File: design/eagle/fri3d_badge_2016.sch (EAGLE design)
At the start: 45 parts

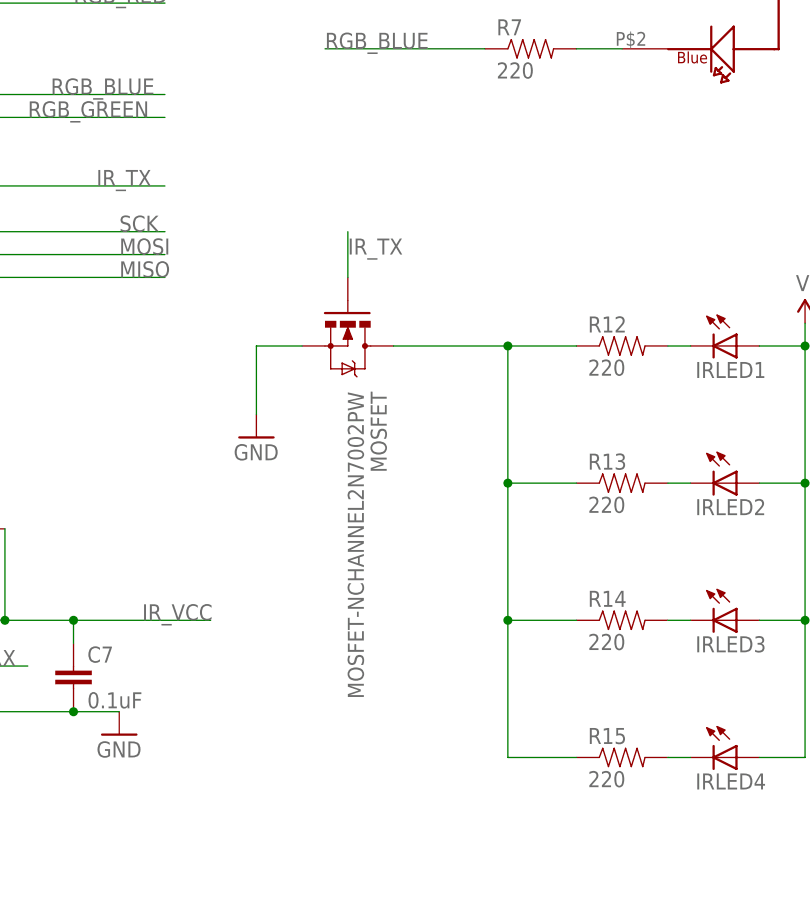
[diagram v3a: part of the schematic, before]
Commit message: fixed MOSFET footprint + added dots for diodes
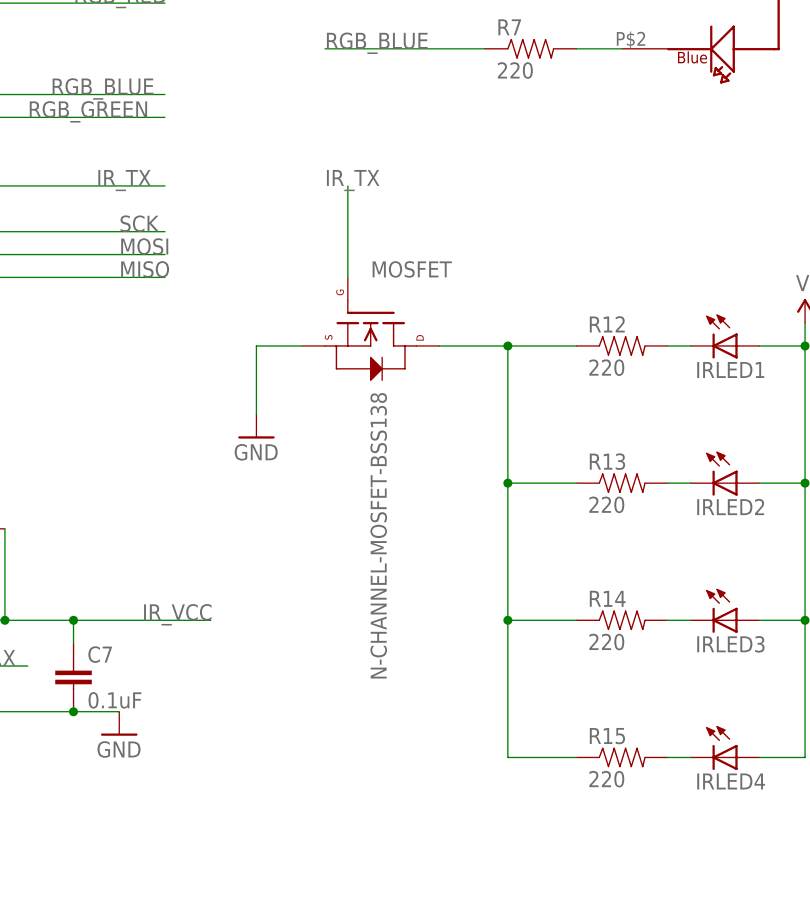
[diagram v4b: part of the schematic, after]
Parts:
- MOSFET: value MOSFET-NCHANNEL2N7002PW -> N-CHANNEL-MOSFET-BSS138; device SparkFun-DiscreteSemi:MOSFET-NCHANNEL2N7002PW -> GeekAmmo:N-CHANNEL-MOSFET-BSS138
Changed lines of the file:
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@@
 <attributes>
 <attribute name="CNAME" value="Fri3d Camp Badge"/>
-<attribute name="CREVISION" value="4"/>
+<attribute name="CREVISION" value="6"/>
 <attribute name="DESIGNER" value="Christophe VG"/>
 </attributes>
@@
 <part name="R14" library="SparkFun-Passives" deviceset="RESISTOR" device="0805-RES" value="220"/>
 <part name="R15" library="SparkFun-Passives" deviceset="RESISTOR" device="0805-RES" value="220"/>
-<part name="MOSFET" library="SparkFun-DiscreteSemi" deviceset="MOSFET-NCHANNEL" device="2N7002PW"/>
 <part name="R5" library="SparkFun-Passives" deviceset="RESISTOR" device="0805-RES" value="220"/>
 <part name="R6" library="SparkFun-Passives" deviceset="RESISTOR" device="0805-RES" value="220"/>
@@
 <part name="SUPPLY9" library="SparkFun-Aesthetics" deviceset="VCC" device=""/>
 <part name="GND13" library="SparkFun-Aesthetics" deviceset="GND" device=""/>
+<part name="MOSFET" library="GeekAmmo" deviceset="N-CHANNEL-MOSFET" device="-BSS138"/>
 </parts>
 <sheets>
@@
 <instance part="R14" gate="G$1" x="193.04" y="40.64"/>
 <instance part="R15" gate="G$1" x="193.04" y="25.4"/>
-<instance part="MOSFET" gate="G$1" x="162.56" y="71.12" rot="R270"/>
 <instance part="R5" gate="G$1" x="205.74" y="154.94"/>
 <instance part="R6" gate="G$1" x="119.38" y="40.64"/>
@@
 <instance part="SUPPLY9" gate="G$1" x="63.5" y="15.24"/>
 <instance part="GND13" gate="1" x="63.5" y="5.08"/>
+<instance part="MOSFET" gate="G$1" x="165.1" y="73.66" smashed="yes" rot="R270">
+<attribute name="VALUE" x="165.1" y="66.04" size="1.778" layer="96" rot="R270"/>
+<attribute name="NAME" x="165.1" y="78.74" size="1.778" layer="95"/>
+</instance>
 </instances>
 <busses>
@@
 </segment>
 <segment>
-<pinref part="GND9" gate="1" pin="GND"/>
-<pinref part="MOSFET" gate="G$1" pin="S"/>
-<wire x1="152.4" y1="63.5" x2="152.4" y2="71.12" width="0.1524" layer="91"/>
-<wire x1="152.4" y1="71.12" x2="157.48" y2="71.12" width="0.1524" layer="91"/>
-</segment>
-<segment>
 <wire x1="-15.24" y1="144.78" x2="-15.24" y2="147.32" width="0.1524" layer="91"/>
 <wire x1="-15.24" y1="147.32" x2="-7.62" y2="147.32" width="0.1524" layer="91"/>
@@
 <wire x1="56.642" y1="10.16" x2="63.5" y2="10.16" width="0.1524" layer="91"/>
 <wire x1="63.5" y1="10.16" x2="63.5" y2="7.62" width="0.1524" layer="91"/>
+</segment>
+<segment>
+<pinref part="GND9" gate="1" pin="GND"/>
+<pinref part="MOSFET" gate="G$1" pin="S"/>
+<wire x1="152.4" y1="63.5" x2="152.4" y2="71.12" width="0.1524" layer="91"/>
+<wire x1="152.4" y1="71.12" x2="157.48" y2="71.12" width="0.1524" layer="91"/>
 </segment>
 </net>
@@
 <net name="IR_TX" class="0">
 <segment>
-<label x="162.56" y="81.28" size="1.778" layer="95"/>
-<pinref part="MOSFET" gate="G$1" pin="G"/>
-<wire x1="162.56" y1="83.82" x2="162.56" y2="78.74" width="0.1524" layer="91"/>
-</segment>
-<segment>
 <pinref part="MCU" gate="G$1" pin="PC7"/>
 <wire x1="106.68" y1="88.9" x2="142.24" y2="88.9" width="0.1524" layer="91"/>
 <label x="134.62" y="88.9" size="1.778" layer="95"/>
+</segment>
+<segment>
+<pinref part="MOSFET" gate="G$1" pin="G"/>
+<wire x1="162.56" y1="78.74" x2="162.56" y2="88.9" width="0.1524" layer="91"/>
+<label x="160.02" y="88.9" size="1.778" layer="95"/>
 </segment>
 </net>
@@
 <pinref part="R13" gate="G$1" pin="1"/>
 <wire x1="187.96" y1="55.88" x2="180.34" y2="55.88" width="0.1524" layer="91"/>
-<pinref part="MOSFET" gate="G$1" pin="D"/>
 <pinref part="R12" gate="G$1" pin="1"/>
-<wire x1="167.64" y1="71.12" x2="180.34" y2="71.12" width="0.1524" layer="91"/>
 <wire x1="180.34" y1="71.12" x2="187.96" y2="71.12" width="0.1524" layer="91"/>
 <wire x1="180.34" y1="55.88" x2="180.34" y2="71.12" width="0.1524" layer="91"/>
-<junction x="180.34" y="71.12"/>
 <wire x1="180.34" y1="40.64" x2="180.34" y2="55.88" width="0.1524" layer="91"/>
 <junction x="180.34" y="55.88"/>
 <wire x1="180.34" y1="25.4" x2="180.34" y2="40.64" width="0.1524" layer="91"/>
 <junction x="180.34" y="40.64"/>
-</segment>
-</net>
+<pinref part="MOSFET" gate="G$1" pin="D"/>
+<wire x1="172.72" y1="71.12" x2="180.34" y2="71.12" width="0.1524" layer="91"/>
+<junction x="180.34" y="71.12"/>
+</segment>
+</net>

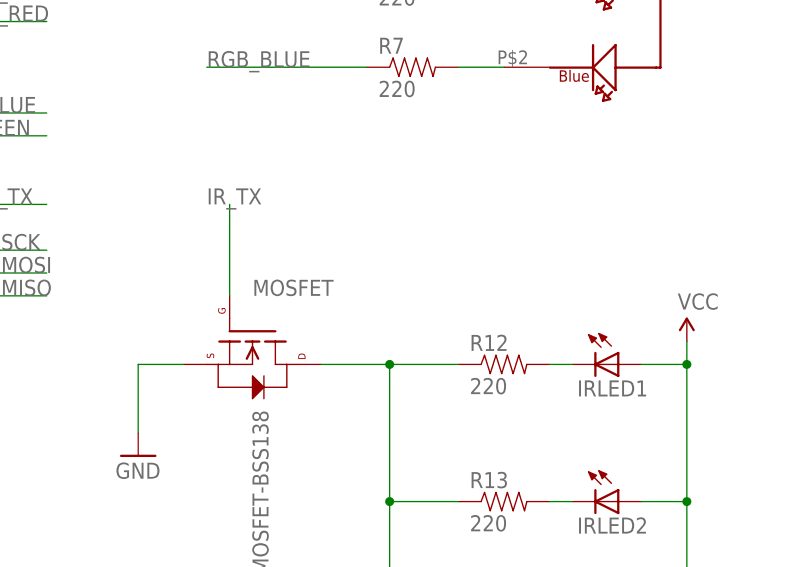
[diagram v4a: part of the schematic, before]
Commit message: added header for IR_TX
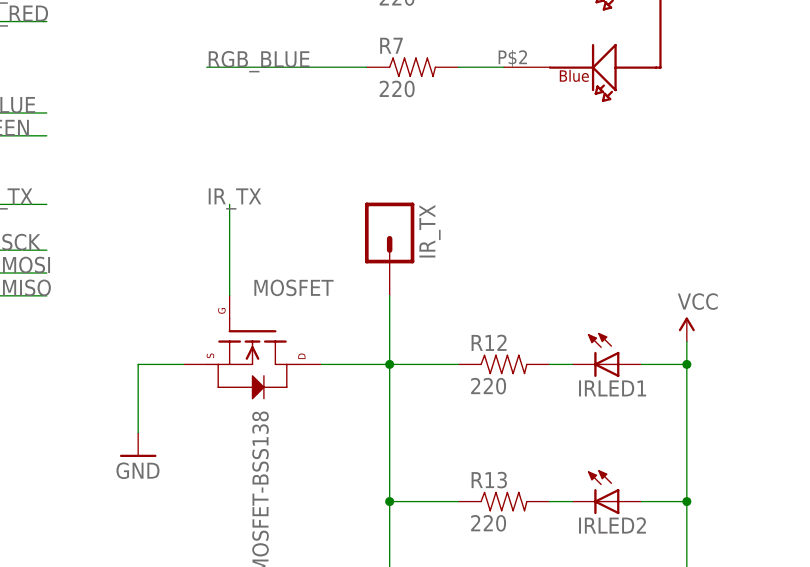
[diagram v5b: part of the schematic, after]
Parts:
- added IR_TX: (no value), SparkFun-Connectors:M01PTH
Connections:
- net N$24: now also IR_TX.1
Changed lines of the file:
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@@
 <part name="GND13" library="SparkFun-Aesthetics" deviceset="GND" device=""/>
 <part name="MOSFET" library="GeekAmmo" deviceset="N-CHANNEL-MOSFET" device="-BSS138"/>
+<part name="IR_TX" library="SparkFun-Connectors" deviceset="M01" device="PTH"/>
 </parts>
 <sheets>
@@
 <attribute name="NAME" x="165.1" y="78.74" size="1.778" layer="95"/>
 </instance>
+<instance part="IR_TX" gate="G$1" x="180.34" y="86.36" rot="R270"/>
 </instances>
 <busses>
@@
 <wire x1="172.72" y1="71.12" x2="180.34" y2="71.12" width="0.1524" layer="91"/>
 <junction x="180.34" y="71.12"/>
-</segment>
-</net>
+<pinref part="IR_TX" gate="G$1" pin="1"/>
+<wire x1="180.34" y1="78.74" x2="180.34" y2="71.12" width="0.1524" layer="91"/>
+</segment>
+</net>
